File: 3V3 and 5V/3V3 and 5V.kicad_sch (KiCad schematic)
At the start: 3 parts, among them U1 AMS1117-3.3

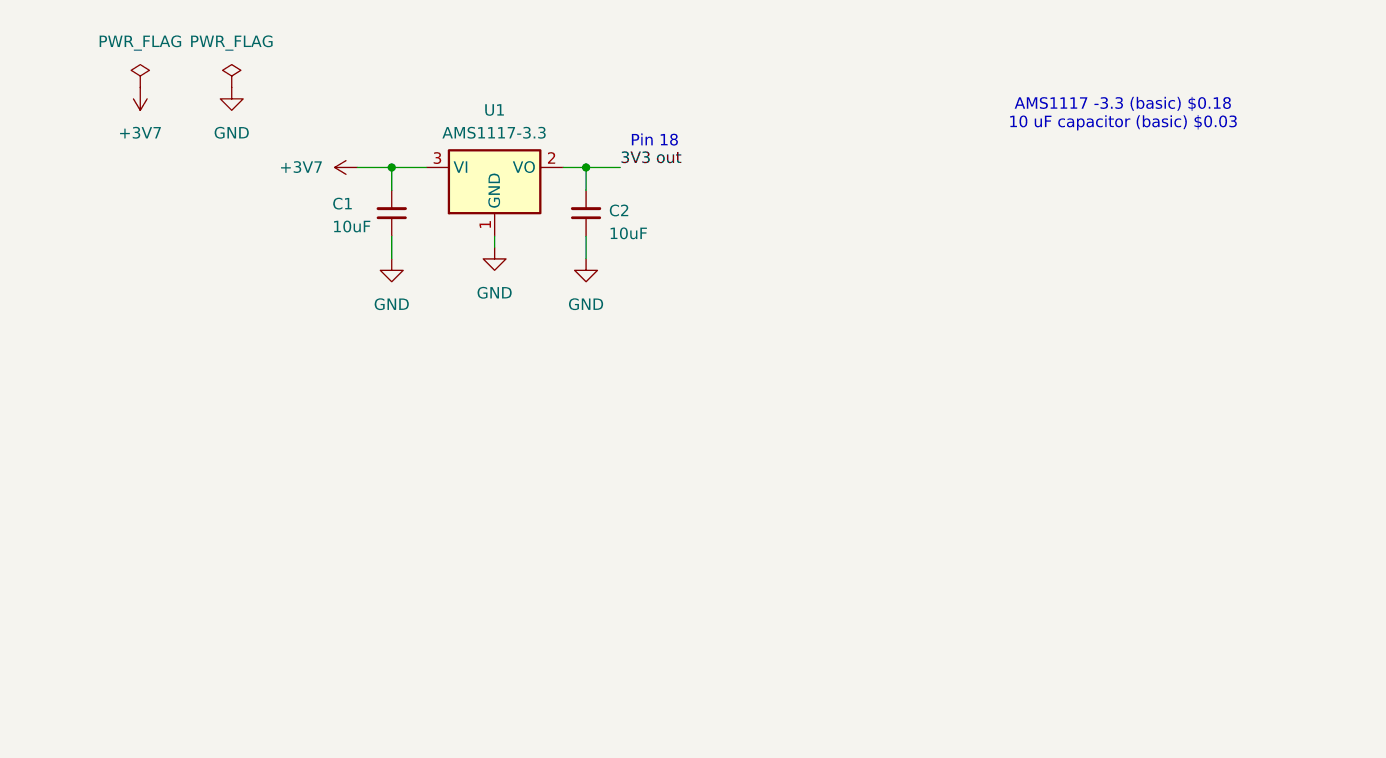
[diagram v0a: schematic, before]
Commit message: Added bidirectional motor control section
Completed the bidirectional motor control part of the system as well as finished the remaining part of the 3V3 and 5V out.
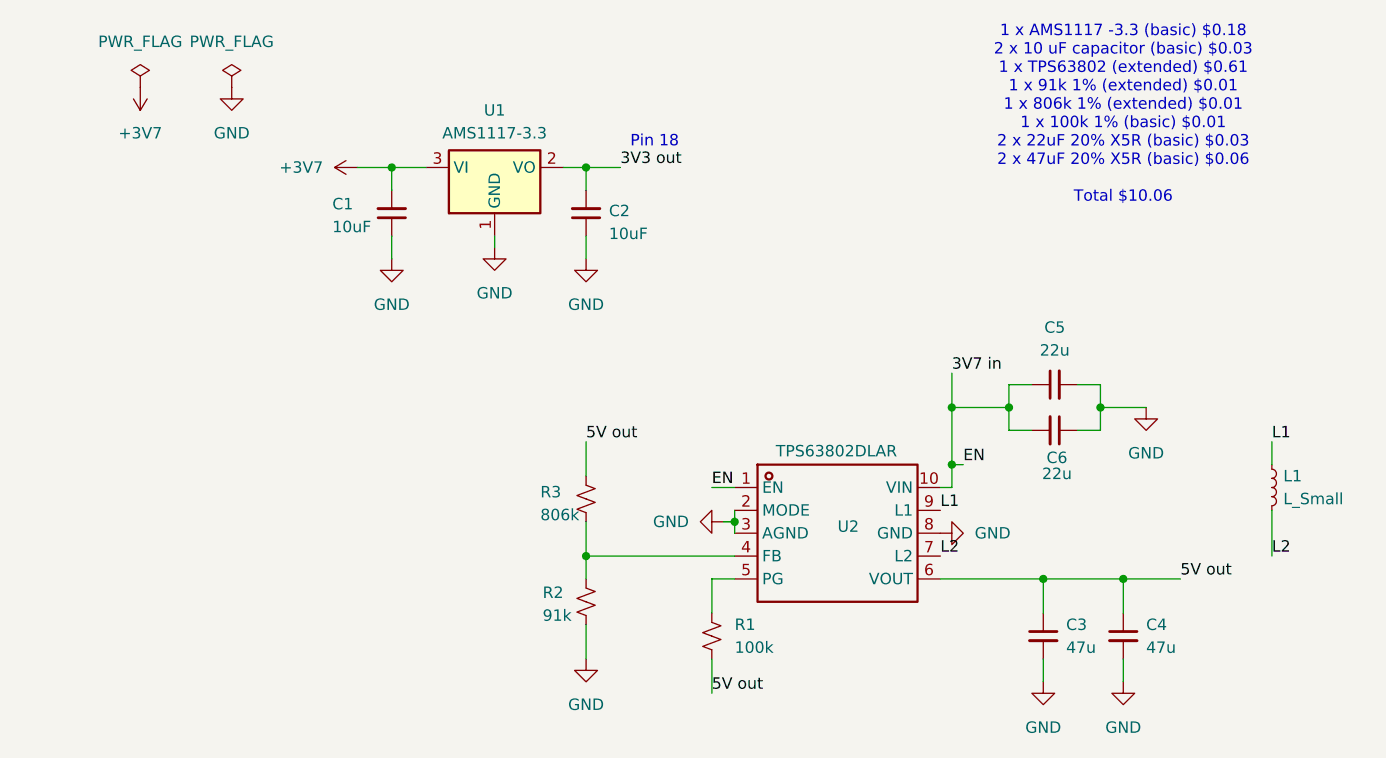
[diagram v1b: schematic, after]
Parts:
- added C3, C4: 47u, symbol Device:C_Small
- added C5, C6: 22u, symbol Device:C_Small
- added L1: L_Small, symbol Device:L_Small
- added R1: 100k, symbol Device:R_Small_US
- added R2: 91k, symbol Device:R_Small_US
- added R3: 806k, symbol Device:R_Small_US
- added U2: TPS63802DLAR, VSON-10_L3.0-W2.0-P0.50-TL, symbol temp-altium-import:root_0_TPS63802DLAR_C2845237
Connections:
- net GND: now also C3.2, C4.2, C5.2, C6.1, R2.1, U2.2 (MODE), U2.3 (AGND), U2.8 (GND)
- new net: R2.2, R3.2, U2.4 (FB)
- new net: R1.1, U2.5 (PG)
- new net 3V7 in: C5.1, C6.2, U2.1 (EN), U2.10 (VIN)
- new net 5V out: C3.1, C4.1, R1.2, R3.1, U2.6 (VOUT)
- new net L1: L1.1, U2.9 (L1)
- new net L2: L1.2, U2.7 (L2)
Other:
- note added: "1 x AMS1117 -3.3 (basic) $0.18 2 x 10 uF capacitor (basic) $0.03 1 x TPS63802 (extended) $0.61 1 x 91k 1% (extended) $0.01 1 x 806k 1% (extended) $0.01 1 x 100k 1% (basic) $0.01 2 x 22uF 20% X5R (basic) $0.03 2 x 47uF 20% X5R (basic) $0.06 Total $10.06"
- note removed: "AMS1117 -3.3 (basic) $0.18 10 uF capacitor (basic) $0.03"

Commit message: ON/OFF switch
Completed the ON/OFF switch.
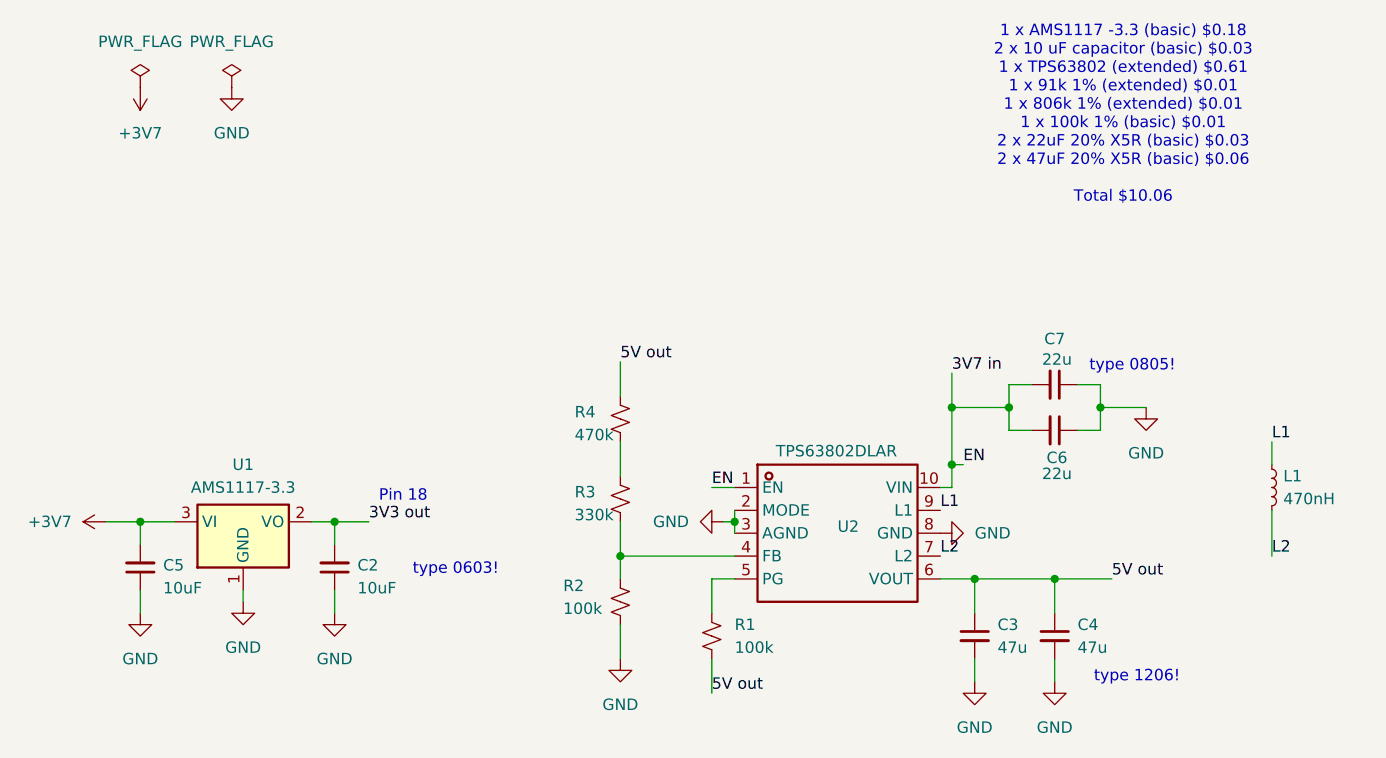
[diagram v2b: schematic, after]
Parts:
- removed C1: 10uF, symbol Device:C_Small
- added C7: 22u, Capacitor_SMD:C_0402_1005Metric_Pad0.74x0.62mm_HandSolder, symbol Device:C_Small
- added R4: 470k, Resistor_SMD:R_0603_1608Metric_Pad0.98x0.95mm_HandSolder, symbol Device:R_Small_US
- C2: footprint (none) -> Capacitor_SMD:C_0402_1005Metric_Pad0.74x0.62mm_HandSolder; LSCS C13585 -> C19702
- C3, C4: footprint (none) -> Capacitor_SMD:C_0402_1005Metric_Pad0.74x0.62mm_HandSolder
- C5: value 22u -> 10uF; footprint (none) -> Capacitor_SMD:C_0402_1005Metric_Pad0.74x0.62mm_HandSolder; LSCS C45783 -> C19702
- C6: footprint (none) -> Capacitor_SMD:C_0402_1005Metric_Pad0.74x0.62mm_HandSolder; LSCS (none) -> C45783
- L1: value L_Small -> 470nH; footprint (none) -> Inductor_SMD:L_0603_1608Metric_Pad1.05x0.95mm_HandSolder; LSCS (none) -> C21307
- R1: footprint (none) -> Resistor_SMD:R_0402_1005Metric_Pad0.72x0.64mm_HandSolder; LSCS C17900 -> C25741
- R2: value 91k -> 100k; footprint (none) -> Resistor_SMD:R_0402_1005Metric_Pad0.72x0.64mm_HandSolder; LSCS C23265 -> C25741
- R3: value 806k -> 330k; footprint (none) -> Resistor_SMD:R_0603_1608Metric_Pad0.98x0.95mm_HandSolder; LSCS C23250 -> C23137
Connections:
- net +3V7: now also C5.2
- net 3V7 in: now also C7.2; no longer C5.1
- net 5V out: now also R4.1; no longer R3.1
- net GND: now also C5.1, R2.2, C7.1; no longer C5.2, R2.1
- net at R3.2, U2.4 (FB): now also R2.1; no longer R2.2
- new net: R3.1, R4.2
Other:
- note added: "type 0603!"
- note added: "type 0805!"
- note added: "type 1206!"
- moved on the sheet: C2, C3, C4, R3, U1
